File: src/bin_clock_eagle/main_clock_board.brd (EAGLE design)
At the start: 51 parts, among them U1 ATMEGA328P-AU, U2 DS1307Z+

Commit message: added v0 gerber files
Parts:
- moved J1 2.84 mm to (5.33, 21.8)
- moved C4 2.54 mm to (9.14, 14.2)
- moved R3 1.80 mm to (20.6, 9.14), turned to 180 degrees
- moved C3 1.27 mm to (9.14, 9.14)
- moved R13 1.27 mm to (58.7, 9.14)
- moved R18 1.27 mm to (46.0, 9.14)
- moved R23 1.27 mm to (51.1, 9.14)
- moved R28 1.27 mm to (38.4, 9.14)
- moved R5 1.27 mm to (63.8, 9.14)
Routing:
- net GND: track 631.0 -> 577.9 mm, vias 4 -> 1
- net N$38: track 64.6 -> 24.9 mm, vias 0 -> 2
- net N$41: track 35.6 -> 54.2 mm, vias 1 -> 0
- net N$42: track 28.9 -> 40.9 mm, vias 2 -> 0
- net VCC: track 647.0 -> 635.9 mm, vias 0 -> 2
- net N$34: track 65.7 -> 76.2 mm, vias 2 -> 1
- net N$14: track 26.0 -> 35.5 mm
- net N$27: track 47.3 -> 40.5 mm
- net N$11: track 48.8 -> 54.8 mm, vias 1 -> 2
- net N$40: track 67.5 -> 61.7 mm
- net N$39: track 69.9 -> 64.8 mm
- net N$23: track 64.5 -> 59.6 mm
- net N$10: track 46.1 -> 41.8 mm
- net N$18: track 66.0 -> 61.8 mm, vias 0 -> 2
- net N$12: track 66.5 -> 62.3 mm, vias 0 -> 2
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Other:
- board text added: "ISP"
- board text added: "MODE"
- board text added: "POWER"
- board text added: "RST"
- board text added: "SERIAL"
- board text added: "SHUT"
- board text added: "SP"
- board text added: "UP DOWN"

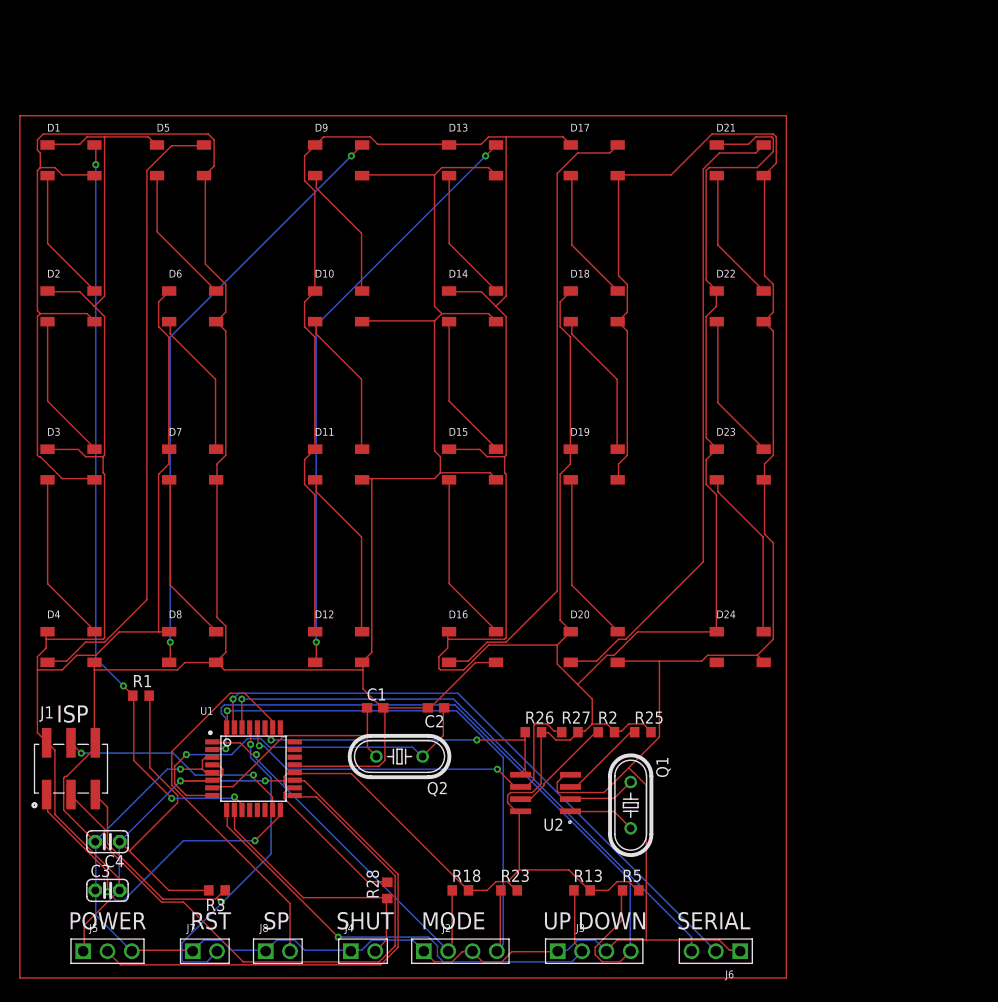
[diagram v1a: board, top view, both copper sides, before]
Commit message: added gound planes
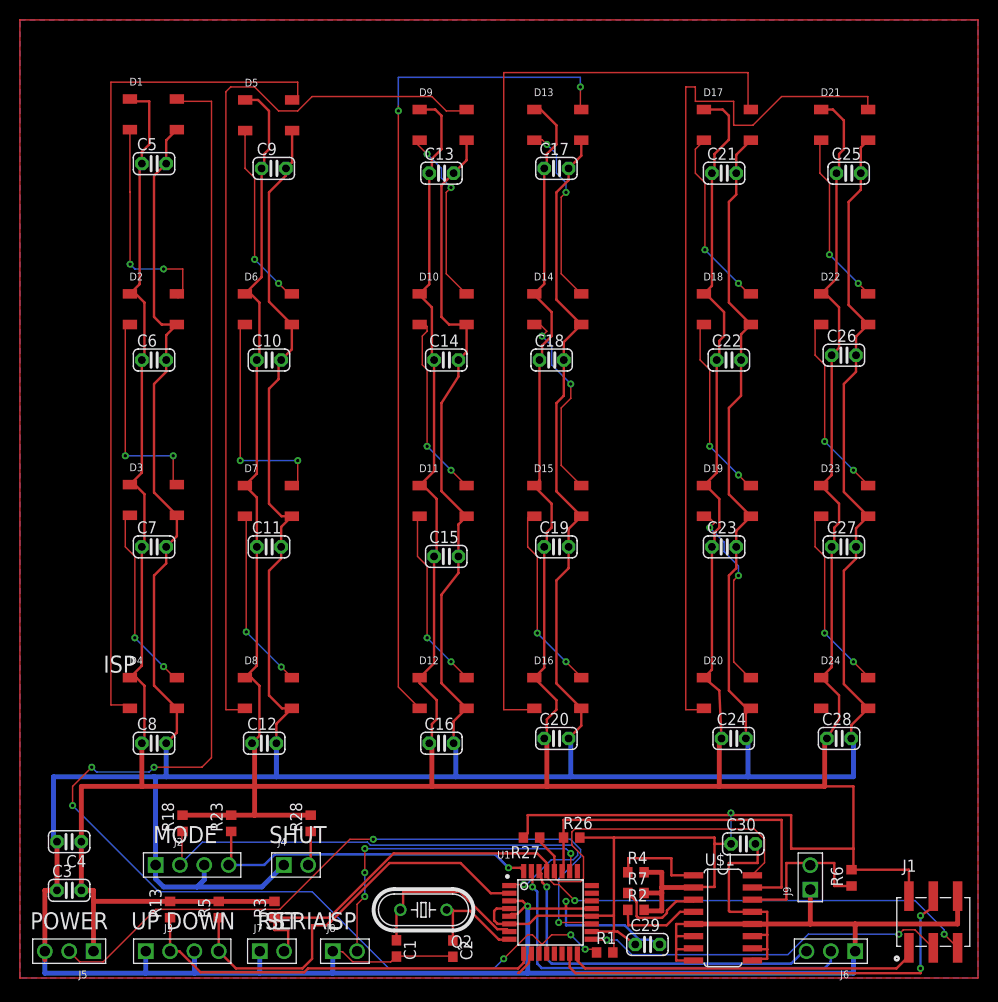
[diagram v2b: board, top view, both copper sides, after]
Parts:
- removed Q1: (no value), adafruit:HC49/S
- removed R25: (no value), adafruit:R0603
- removed U2: DS1307Z+, DS1307Z_:SO08
- added C10, C11, C12, C13, C14, C15, C16, C17, C18, C19, C20, C21, C22, C23, C24, C25, C26, C27, C28, C29, C30, C5, C6, C7, C8, C9: 100n, adafruit:C025-024X044
- added J9: (no value), Wurth_Elektronik_Electromechanic_Board_to_Board_Connectors_rev16c:61300211121
- added R4, R7: 5k, adafruit:R0603
- added R6: 220, adafruit:R0603
- added U$1: DS3231, DS3231:SO16
- C1, C2: value (none) -> 22p
- C3, C4: value (none) -> 100n
- Q2: value (none) -> 16mhz
- R1, R26, R27: value (none) -> 10k
- R13, R18, R2, R23, R28, R3, R5: value (none) -> 5k
- moved J1 91.4 mm to (95.3, 5.84)
- moved R1 55.3 mm to (61.0, 2.66)
- moved R13 43.0 mm to (15.7, 7.14), turned to 90 degrees
- moved R5 43.0 mm to (20.8, 7.14), turned to 90 degrees
- moved J3 43.0 mm to (16.9, 2.79)
- moved U1 34.4 mm to (55.4, 6.84)
- moved R23 29.8 mm to (22.1, 16.1), turned to 90 degrees
- moved R18 29.8 mm to (17.0, 16.1), turned to 90 degrees
- moved J2 29.4 mm to (18.0, 11.8)
- moved C1 25.2 mm to (39.3, 3.08), turned to 270 degrees
- moved C2 25.2 mm to (45.2, 3.07), turned to 270 degrees
- moved R2 18.8 mm to (64.3, 7.11)
- moved Q2 16.2 mm to (42.1, 7.11)
- moved D20 14.7 mm to (73.8, 29.7)
- moved D19 14.4 mm to (73.8, 49.8)
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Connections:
- removed net N$22: R25.1, U2.3
- new net N$15: R2.1, U$1.4
- net GND: now also C10.2, C11.2, C12.2, C13.2, C14.2, C15.2, C16.2, C17.2, C18.2, C19.2, C20.2, C21.2, C22.2, C23.2, C24.2, C25.2, C26.2, C27.2, C28.2, C29.2, C30.2, C5.2, C6.2, C7.2, C8.2, C9.2, J9.1, U$1.10, U$1.11, U$1.12, U$1.13, U$1.5, U$1.6, U$1.7, U$1.8, U$1.9; no longer U2.4
- net N$10: now also U$1.16; no longer U2.6
- net N$2: now also U$1.15; no longer U2.5
- net N$43: now also R4.1, U$1.1; no longer Q1.2, U2.1
- net N$44: now also J9.2, R6.1, U$1.14; no longer Q1.1, U2.2
- net N$45: now also R7.1, U$1.3; no longer R2.1, U2.7
- net VCC: now also C10.1, C11.1, C12.1, C13.1, C14.1, C15.1, C16.1, C17.1, C18.1, C19.1, C20.1, C21.1, C22.1, C23.1, C24.1, C25.1, C26.1, C27.1, C28.1, C29.1, C30.1, C5.1, C6.1, C7.1, C8.1, C9.1, R4.2, R6.2, R7.2, U$1.2; no longer R25.2, U2.8
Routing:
- net GND: track 577.9 -> 794.3 mm, vias 1 -> 2
- net VCC: track 635.9 -> 733.8 mm, vias 2 -> 1
- net N$36: track 79.9 -> 156.5 mm, vias 4 -> 6
- net N$3: track 340.0 -> 400.0 mm
- net N$24: track 65.6 -> 100.3 mm
- net N$34: track 76.2 -> 42.5 mm, vias 1 -> 0
- net N$12: track 62.3 -> 94.3 mm, vias 2 -> 0
- net N$11: track 54.8 -> 84.7 mm
- net N$47: track 40.2 -> 11.8 mm, vias 1 -> 0
- net N$18: track 61.8 -> 89.9 mm
- net N$30: track 66.5 -> 92.7 mm
- net N$26: track 64.1 -> 38.2 mm, vias 0 -> 2
- net N$40: track 61.7 -> 37.3 mm
- net N$6: track 65.0 -> 89.3 mm
- net N$23: track 59.6 -> 35.8 mm
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- added copper zone on layer 16, net N$22
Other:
- board text added: "BATT"

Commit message: DRC check ok
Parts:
- moved C1 6.66 mm to (40.1, 9.69), turned to 180 degrees
- moved C2 5.18 mm to (40.1, 3.81), turned to 180 degrees
- moved R4 4.92 mm to (68.8, 13.0)
- moved R7 4.00 mm to (64.3, 12.9), turned to 180 degrees
- moved C29 3.50 mm to (65.5, 7.00)
- moved R2 3.00 mm to (64.3, 10.1), turned to 180 degrees
- moved R1 2.55 mm to (63.5, 3.16)
- moved Q2 2.00 mm to (44.1, 6.88), turned to 90 degrees
- moved C13 1.00 mm to (44.0, 85.0)
- moved C17 1.00 mm to (56.0, 85.5)
- moved C21 1.00 mm to (73.5, 85.0)
- moved C25 1.00 mm to (86.5, 85.0)
- moved D13 1.00 mm to (56.1, 90.0)
- moved D17 1.00 mm to (73.8, 90.0)
- moved D21 1.00 mm to (86.1, 90.0)
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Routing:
- net N$37: track 6.43 -> 46.1 mm, vias 0 -> 5
- net N$35: track 42.7 -> 48.7 mm, vias 0 -> 2
- net N$43: track 10.1 -> 4.35 mm
- net N$46: track 18.6 -> 12.9 mm
- net N$36: track 156.5 -> 159.3 mm
- net N$15: track 9.00 -> 6.43 mm
- net GND: track 794.3 -> 796.7 mm
- net N$34: track 42.5 -> 44.9 mm
- net N$12: track 94.3 -> 96.6 mm
- net VCC: track 733.8 -> 731.8 mm
- net N$45: track 9.85 -> 7.99 mm
- net N$26: track 38.2 -> 36.8 mm
- net N$24: track 100.3 -> 99.0 mm
- net N$31: track 18.1 -> 19.1 mm
- net N$30: track 92.7 -> 93.7 mm
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- added copper zone on layer 16, net VGND
- removed copper zone on layer 16, net N$22

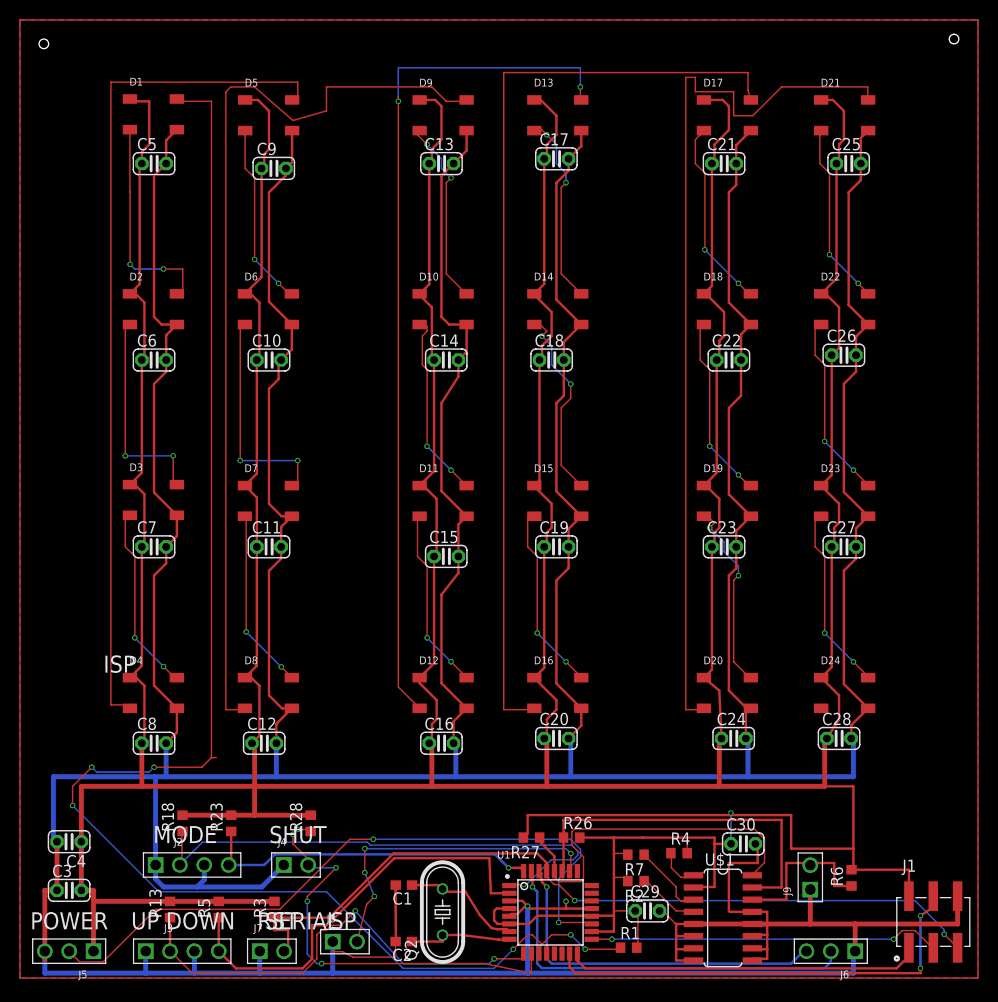
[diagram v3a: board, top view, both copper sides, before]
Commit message: skilscreen correction
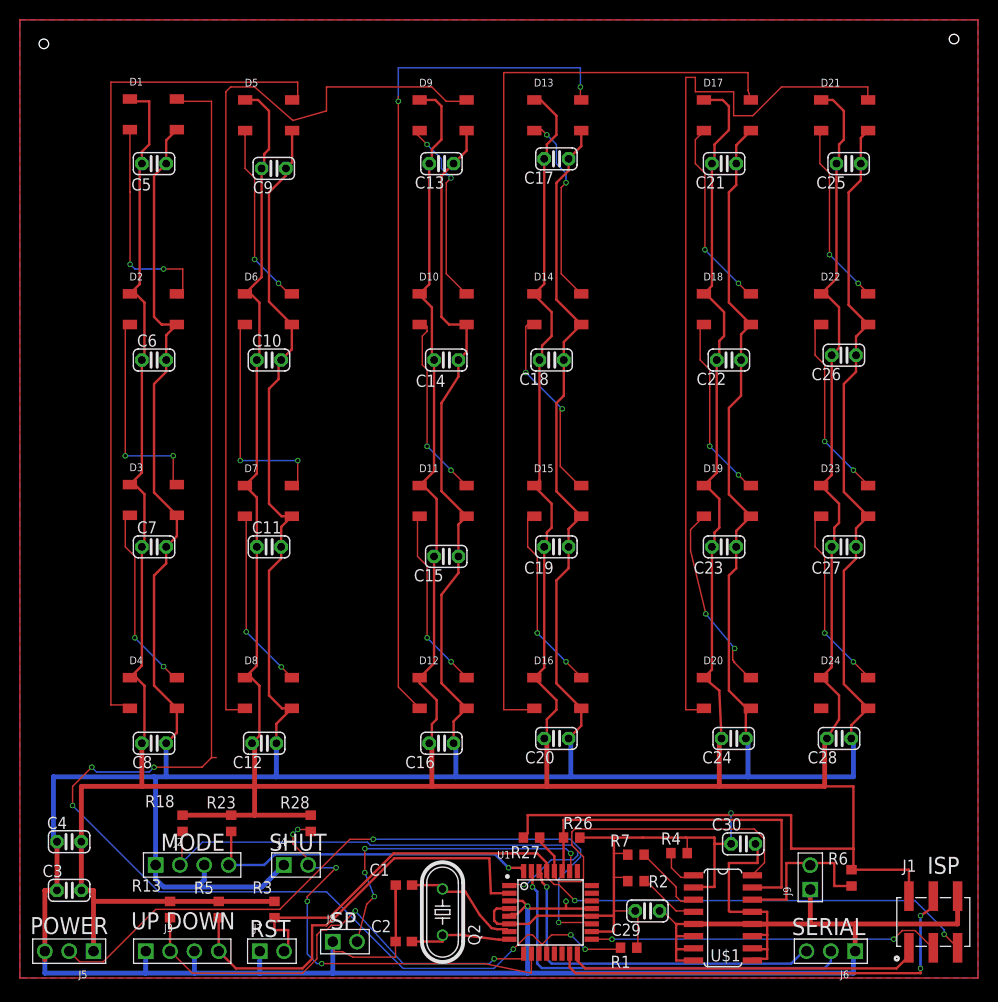
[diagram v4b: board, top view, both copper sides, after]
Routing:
- net N$29: track 20.3 -> 19.7 mm

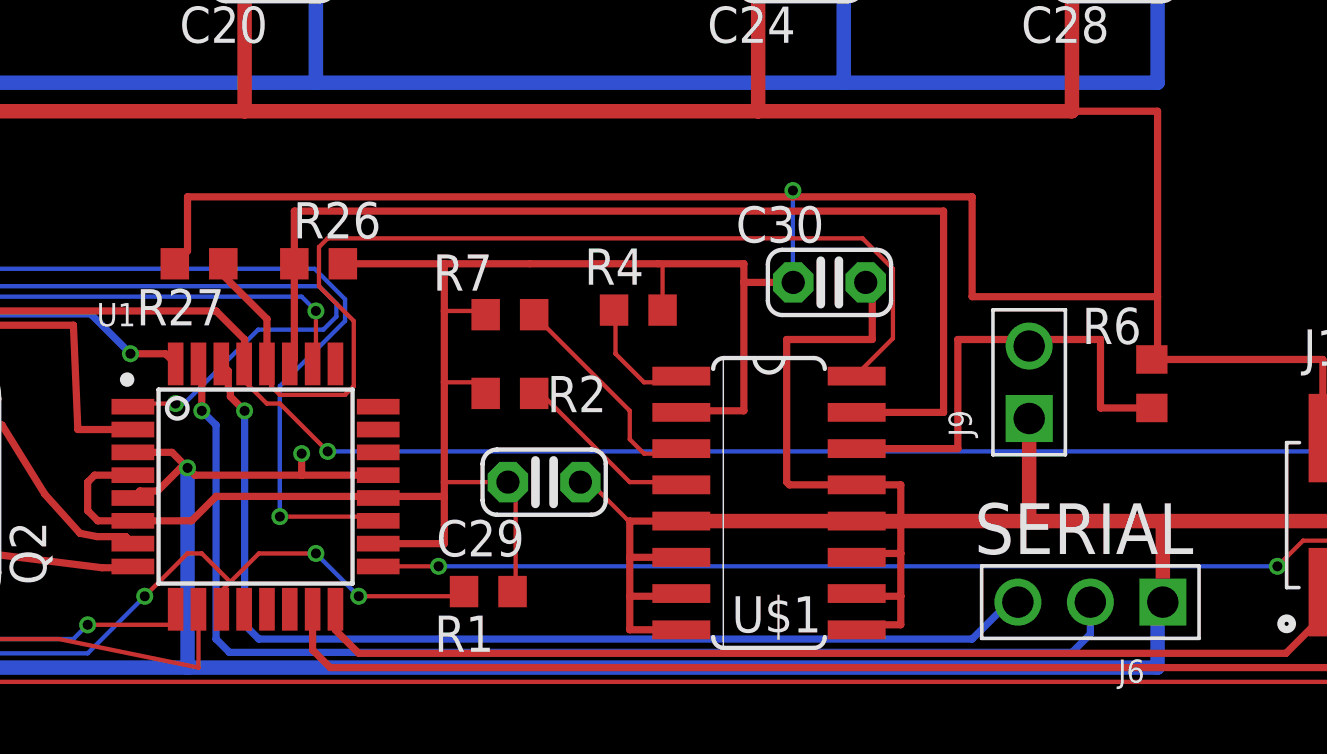
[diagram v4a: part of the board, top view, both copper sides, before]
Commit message: fixed ds3231 package to SO16W
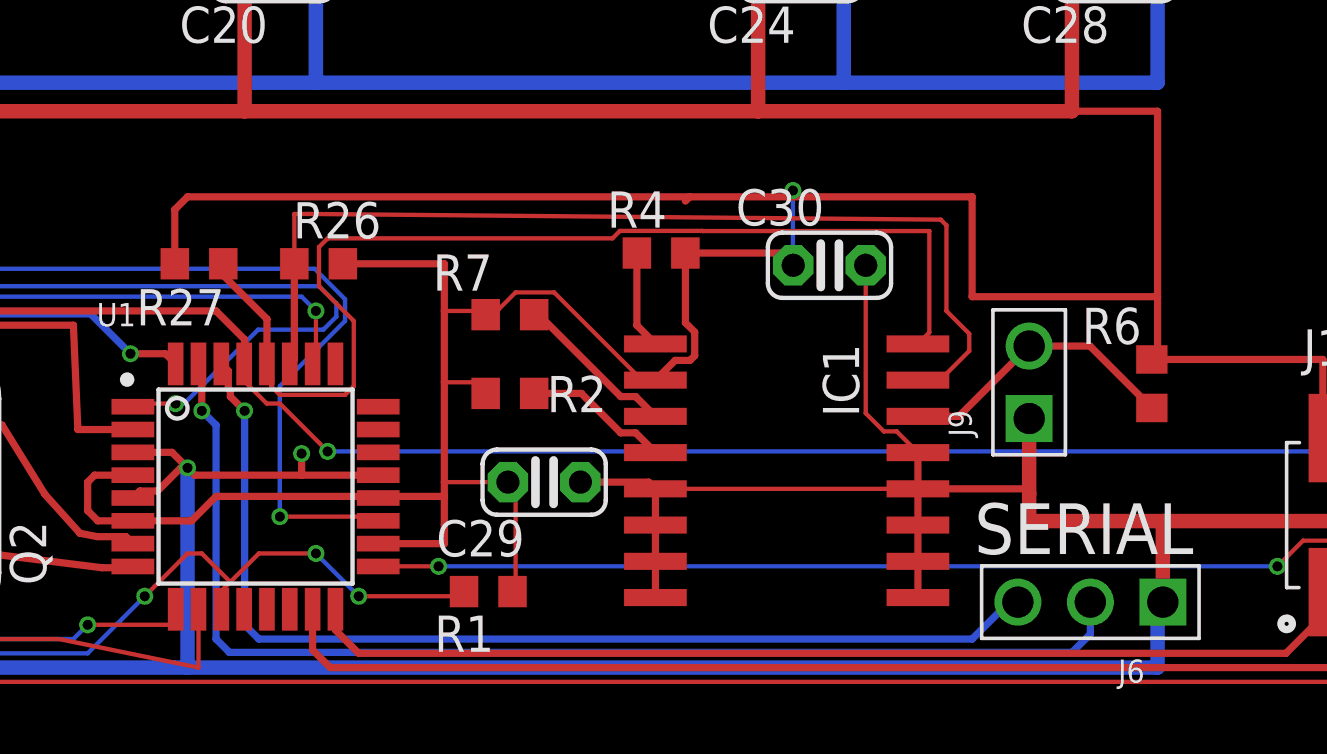
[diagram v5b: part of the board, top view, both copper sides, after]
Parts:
- removed U$1: DS3231, DS3231:SO16
- added IC1: DS3231/SO, DS3231_so16w:SO16W
- moved R4 2.15 mm to (69.6, 15.0)
- moved C30 0.60 mm to (75.5, 14.6)
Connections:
- net GND: now also IC1.10, IC1.11, IC1.12, IC1.13, IC1.5, IC1.6, IC1.7, IC1.8, IC1.9; no longer U$1.10, U$1.11, U$1.12, U$1.13, U$1.5, U$1.6, U$1.7, U$1.8, U$1.9
- net N$10: now also IC1.16; no longer U$1.16
- net N$15: now also IC1.4; no longer U$1.4
- net N$2: now also IC1.15; no longer U$1.15
- net N$43: now also IC1.1; no longer U$1.1
- net N$44: now also IC1.14; no longer U$1.14
- net N$45: now also IC1.3; no longer U$1.3
- net VCC: now also IC1.2; no longer U$1.2
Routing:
- net GND: track 796.7 -> 777.7 mm
- net N$44: track 16.8 -> 10.1 mm
- net VCC: track 731.8 -> 728.1 mm
- net N$2: track 38.3 -> 35.2 mm
- net N$45: track 7.99 -> 5.73 mm
- net N$15: track 6.43 -> 5.48 mm
- net N$43: track 4.35 -> 3.45 mm
- net N$10: track 38.5 -> 39.3 mm
